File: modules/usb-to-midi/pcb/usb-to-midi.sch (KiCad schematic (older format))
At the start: 22 parts, among them J1 USB_B, J2 MIDI out, J3 DEBUG HEADER, U1 ATmega32U2-AU, Y1 16mhz

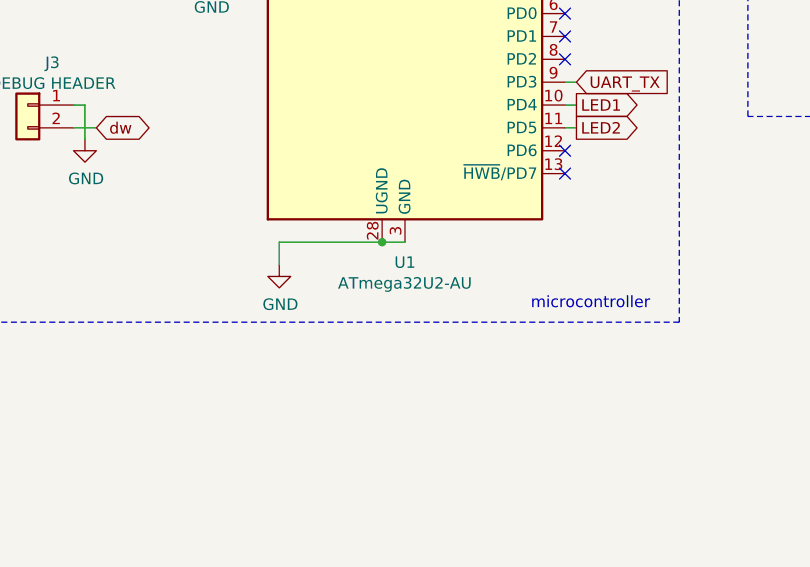
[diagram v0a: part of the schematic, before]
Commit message: usb-to-midi: fix some metadata, add schematic pdf
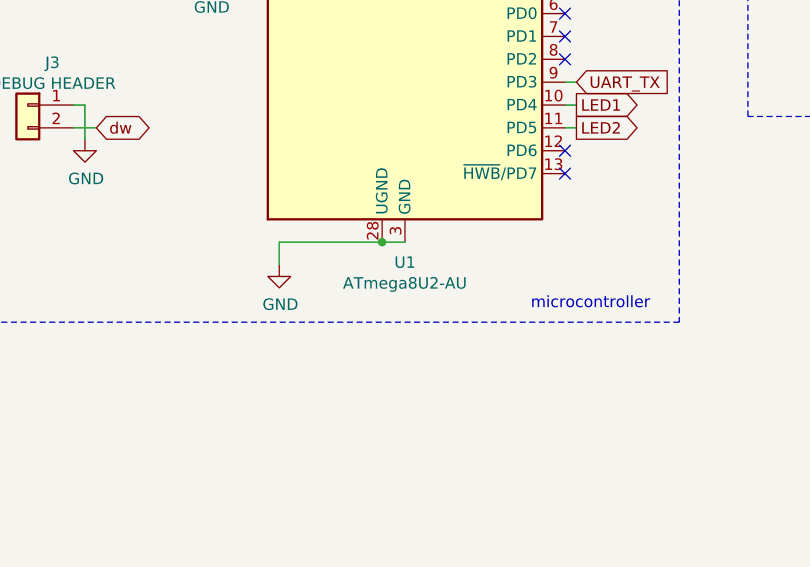
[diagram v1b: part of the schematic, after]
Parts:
- U1: value ATmega32U2-AU -> ATmega8U2-AU
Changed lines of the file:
@@
 encoding utf-8
 Sheet 1 1
-Title "usb-to-midi board"
+Title "usb-to-midi"
 Date "2021-12-13"
 Rev "1.0"
@@
 P 5800 3700
 F 0 "U1" H 5800 2211 50  0000 C CNN
-F 1 "ATmega32U2-AU" H 5800 2120 50  0000 C CNN
+F 1 "ATmega8U2-AU" H 5800 2120 50  0000 C CNN
 F 2 "eurorack:TQFP-32_7x7mm_P0.8mm_LongPads" H 5800 3700 50  0001 C CIN
 F 3 "http://ww1.microchip.com/downloads/en/DeviceDoc/doc7799.pdf" H 5800 3700 50  0001 C CNN

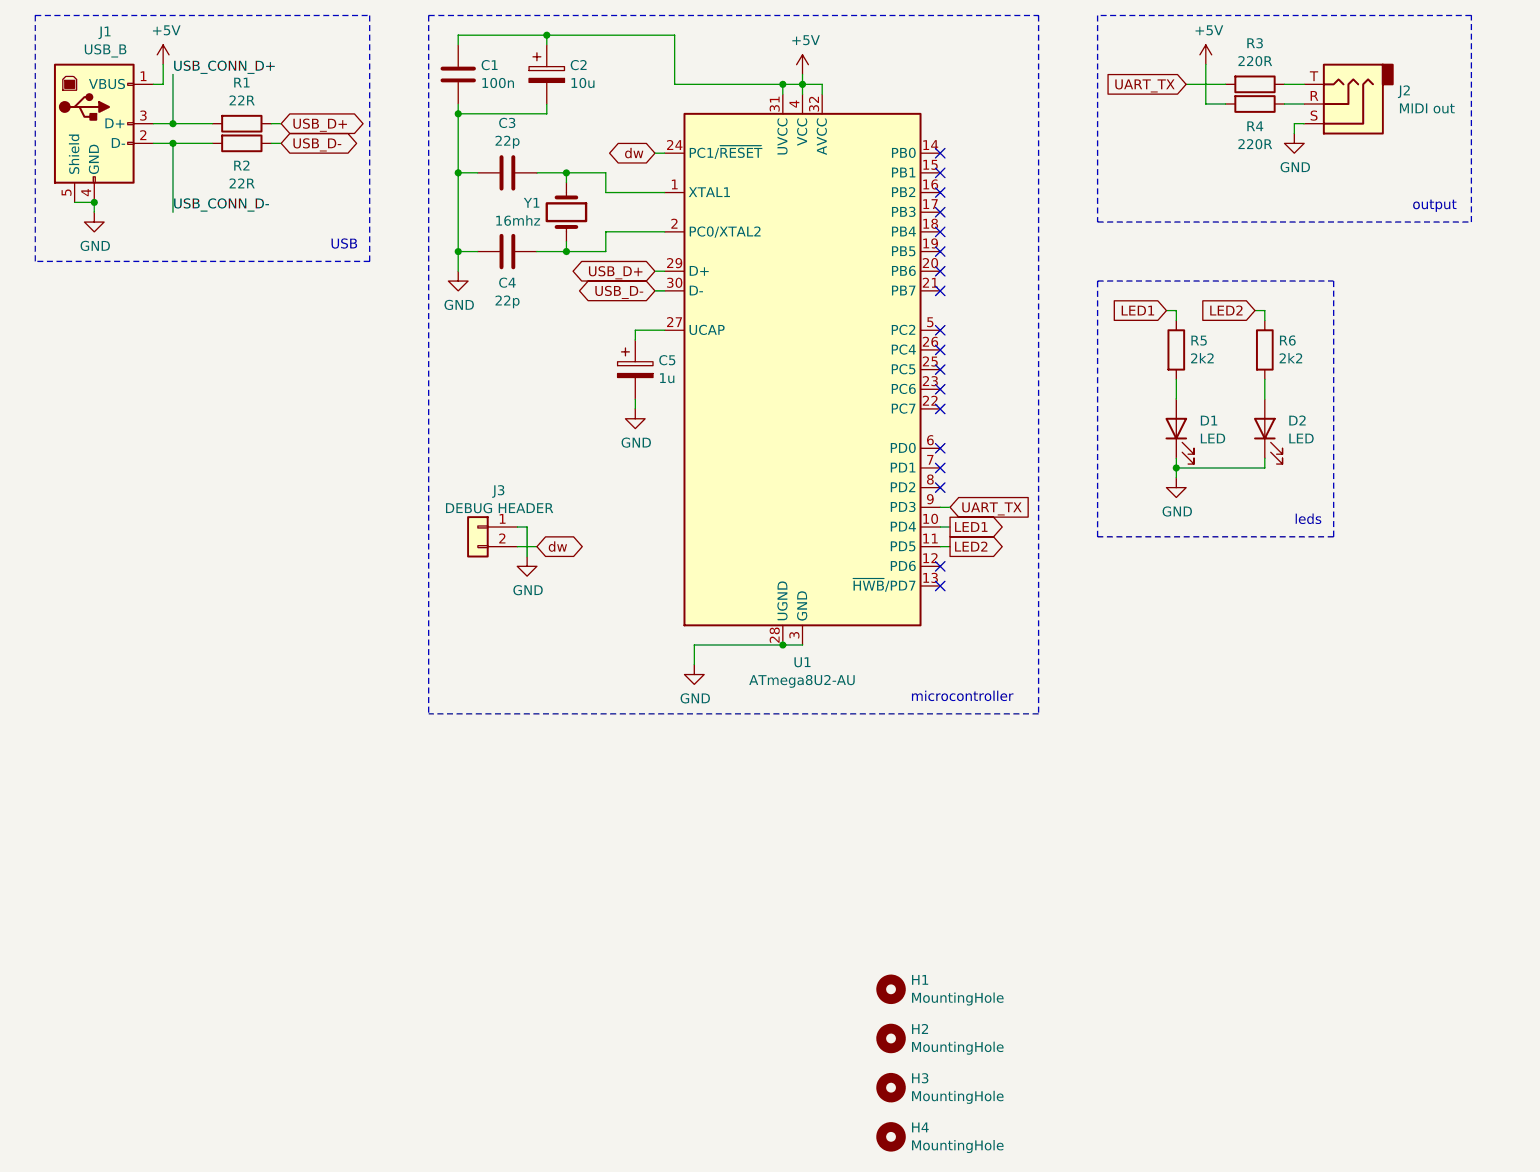
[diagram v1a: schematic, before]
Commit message: modules: usb-to-midi: fix references
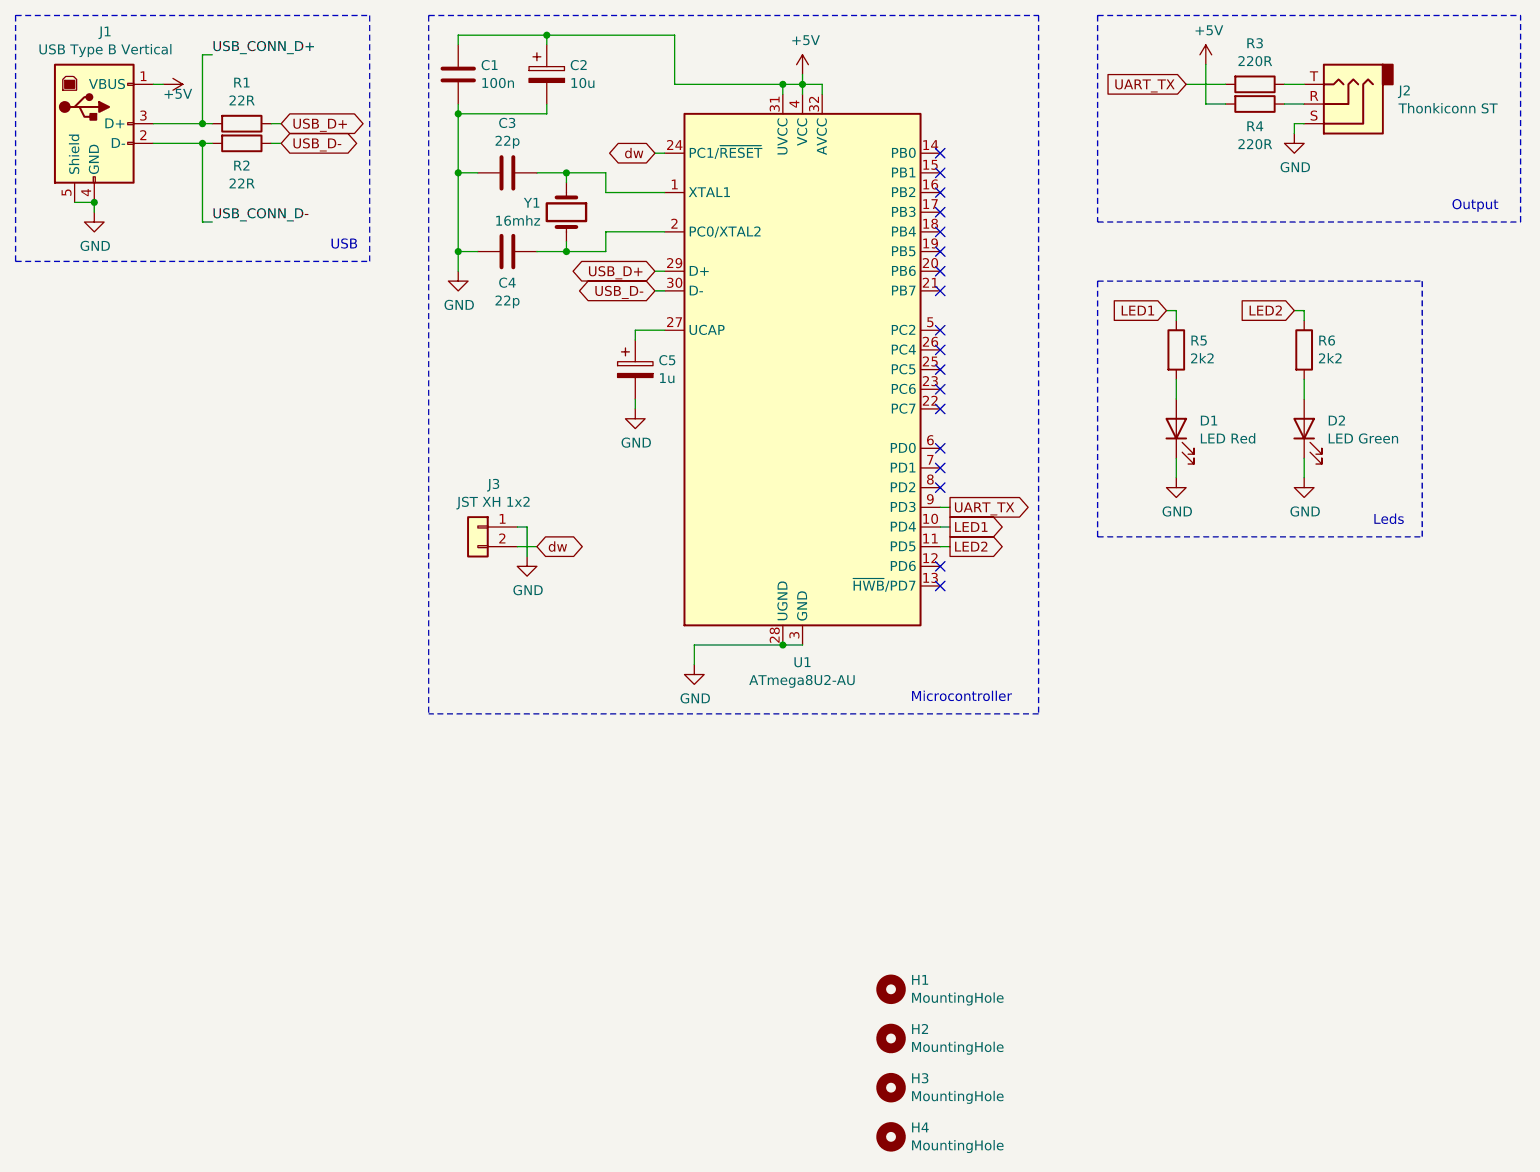
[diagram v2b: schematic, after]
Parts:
- D1: value LED -> LED Red
- D2: value LED -> LED Green
- J1: value USB_B -> USB Type B Vertical
- J2: value MIDI out -> Thonkiconn ST
- J3: value DEBUG HEADER -> JST XH 1x2
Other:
- note added: "Leds"
- note added: "Microcontroller"
- note added: "Output"
- note removed: "leds"
- note removed: "microcontroller"
- note removed: "output"
- moved on the sheet: D2, R6
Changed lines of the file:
@@
 	0    1    1    0
 $EndComp
-Text GLabel 6550 4400 2    50   Input ~ 0
+Text GLabel 6550 4400 2    50   Output ~ 0
 UART_TX
 $Comp
@@
 U 1 1 61353B09
 P 4150 4500
-F 0 "J3" H 4042 4685 50  0000 C CNN
-F 1 "DEBUG HEADER" H 4042 4594 50  0000 C CNN
+F 0 "J3" H 4068 4717 50  0000 C CNN
+F 1 "JST XH 1x2" H 4068 4626 50  0000 C CNN
 F 2 "Connector_JST:JST_XH_B2B-XH-A_1x02_P2.50mm_Vertical" H 4150 4500 50  0001 C CNN
 F 3 "~" H 4150 4500 50  0001 C CNN
@@
 P 7700 4000
 F 0 "D1" V 7739 3882 50  0000 R CNN
-F 1 "LED" V 7648 3882 50  0000 R CNN
+F 1 "LED Red" V 7648 3882 50  0000 R CNN
 F 2 "LED_THT:LED_D3.0mm" H 7700 4000 50  0001 C CNN
 F 3 "~" H 7700 4000 50  0001 C CNN
@@
 L Device:LED D2
 U 1 1 61C75707
-P 8150 4000
-F 0 "D2" V 8189 3882 50  0000 R CNN
-F 1 "LED" V 8098 3882 50  0000 R CNN
-F 2 "LED_THT:LED_D3.0mm" H 8150 4000 50  0001 C CNN
-F 3 "~" H 8150 4000 50  0001 C CNN
-	1    8150 4000
+P 8350 4000
+F 0 "D2" V 8389 3882 50  0000 R CNN
+F 1 "LED Green" V 8298 3882 50  0000 R CNN
+F 2 "LED_THT:LED_D3.0mm" H 8350 4000 50  0001 C CNN
+F 3 "~" H 8350 4000 50  0001 C CNN
+	1    8350 4000
 	0    -1   -1   0
 $EndComp
@@
 L Device:R R6
 U 1 1 61C770E0
-P 8150 3600
-F 0 "R6" H 8220 3646 50  0000 L CNN
-F 1 "2k2" H 8220 3555 50  0000 L CNN
-F 2 "Resistor_THT:R_Axial_DIN0207_L6.3mm_D2.5mm_P10.16mm_Horizontal" V 8080 3600 50  0001 C CNN
-F 3 "~" H 8150 3600 50  0001 C CNN
-	1    8150 3600
+P 8350 3600
+F 0 "R6" H 8420 3646 50  0000 L CNN
+F 1 "2k2" H 8420 3555 50  0000 L CNN
+F 2 "Resistor_THT:R_Axial_DIN0207_L6.3mm_D2.5mm_P10.16mm_Horizontal" V 8280 3600 50  0001 C CNN
+F 3 "~" H 8350 3600 50  0001 C CNN
+	1    8350 3600
 	1    0    0    -1
 $EndComp
 Text GLabel 7650 3400 0    50   Input ~ 0
 LED1
-Text GLabel 8100 3400 0    50   Input ~ 0
+Text GLabel 8300 3400 0    50   Input ~ 0
 LED2
 $Comp
@@
 	7700 3400 7700 3450
 Wire Wire Line
-	8100 3400 8150 3400
-Wire Wire Line
-	8150 3400 8150 3450
+	8300 3400 8350 3400
+Wire Wire Line
+	8350 3400 8350 3450
 Wire Wire Line
 	7700 3850 7700 3750
 Wire Wire Line
-	8150 3750 8150 3850
-Wire Wire Line
-	7700 4250 7700 4200
-Wire Wire Line
-	7700 4200 8150 4200
-Wire Wire Line
-	8150 4200 8150 4150
-Connection ~ 7700 4200
-Wire Wire Line
-	7700 4200 7700 4150
+	8350 3750 8350 3850
 NoConn ~ 6500 4200
 NoConn ~ 6500 4100
@@
 NoConn ~ 6500 3100
 NoConn ~ 6500 3600
-Text Notes 8900 2900 0    50   ~ 0
-output
-Wire Notes Line
-	8500 3250 8500 4550
-Text Notes 8300 4500 0    50   ~ 0
-leds
+Text Notes 9100 2900 0    50   ~ 0
+Output
+Wire Notes Line
+	8950 3250 8950 4550
+Text Notes 8700 4500 0    50   ~ 0
+Leds
 Wire Notes Line
 	7000 5450 3900 5450
@@
 Connection ~ 5700 5100
 Text Notes 6350 5400 0    50   ~ 0
-microcontroller
-Wire Notes Line
-	1900 1900 3600 1900
+Microcontroller
 Wire Notes Line
 	3600 1900 3600 3150
 Wire Notes Line
-	3600 3150 1900 3150
-Wire Notes Line
-	1900 3150 1900 1900
+	1800 3150 1800 1900
 Text Notes 3400 3100 0    50   ~ 0
 USB
-Text Label 2600 2200 0    50   ~ 0
+Text Label 2800 2100 0    50   ~ 0
 USB_CONN_D+
 Connection ~ 2200 2850
@@
 AR Path="/6175D50F/61C21FC1" Ref="J?"  Part="1"
 F 0 "J1" H 2257 2917 50  0000 C CNN
-F 1 "USB_B" H 2257 2826 50  0000 C CNN
+F 1 "USB Type B Vertical" H 2257 2826 50  0000 C CNN
 F 2 "eurorack:USB_B_Vertical" H 2350 2400 50  0001 C CNN
 F 3 " ~" H 2350 2400 50  0001 C CNN
@@
 	1    0    0    -1
 $EndComp
-Text Label 2600 2900 0    50   ~ 0
+Text Label 2800 2950 0    50   ~ 0
 USB_CONN_D-
-Wire Wire Line
-	2600 2900 2600 2550
-Wire Wire Line
-	2600 2550 2500 2550
-Wire Wire Line
-	2800 2550 2600 2550
-Connection ~ 2600 2550
-Wire Wire Line
-	2500 2450 2600 2450
-Wire Wire Line
-	2600 2200 2600 2450
-Connection ~ 2600 2450
-Wire Wire Line
-	2600 2450 2800 2450
 $Comp
 L power:GND #PWR0103
@@
 P 8550 2350
 F 0 "J2" H 8270 2283 50  0000 R CNN
-F 1 "MIDI out" H 8270 2374 50  0000 R CNN
+F 1 "Thonkiconn ST" H 8270 2374 50  0000 R CNN
 F 2 "eurorack:Jack_3.5mm_QingPu_WQP-PJ366ST_Vertical" H 8550 2350 50  0001 C CNN
 F 3 "~" H 8550 2350 50  0001 C CNN
@@
 NoConn ~ 6500 4800
 Wire Notes Line
-	9200 2950 9200 1900
-Wire Notes Line
-	9200 1900 7300 1900
+	9450 2950 9450 1900
 Wire Notes Line
 	7300 1900 7300 2950
 Wire Notes Line
-	7300 2950 9200 2950
-Wire Notes Line
-	8500 4550 7300 4550
-Wire Notes Line
 	7300 4550 7300 3250
-Wire Notes Line
-	7300 3250 8500 3250
-$Comp
-L power:+5V #PWR0107
-U 1 1 61655010
-P 2550 2150
-F 0 "#PWR0107" H 2550 2000 50  0001 C CNN
-F 1 "+5V" H 2565 2323 50  0000 C CNN
-F 2 "" H 2550 2150 50  0001 C CNN
-F 3 "" H 2550 2150 50  0001 C CNN
-	1    2550 2150
-	1    0    0    -1
-$EndComp
 Wire Wire Line
 	2500 2250 2550 2250
-Wire Wire Line
-	2550 2250 2550 2150
 Wire Wire Line
 	6500 4600 6550 4600
@@
 Wire Notes Line
 	3900 1900 3900 5450
+Wire Wire Line
+	2500 2550 2750 2550
+Wire Wire Line
+	2500 2450 2750 2450
+$Comp
+L power:+5V #PWR0107
+U 1 1 61655010
+P 2550 2250
+F 0 "#PWR0107" H 2550 2100 50  0001 C CNN
+F 1 "+5V" V 2600 2250 50  0000 L CNN
+F 2 "" H 2550 2250 50  0001 C CNN
+F 3 "" H 2550 2250 50  0001 C CNN
+	1    2550 2250
+	0    1    1    0
+$EndComp
+Wire Wire Line
+	2750 2450 2750 2100
+Wire Wire Line
+	2750 2100 2800 2100
+Connection ~ 2750 2450
+Wire Wire Line
+	2750 2450 2800 2450
+Wire Wire Line
+	2750 2550 2750 2950
+Wire Wire Line
+	2750 2950 2800 2950
+Connection ~ 2750 2550
+Wire Wire Line
+	2750 2550 2800 2550
+Wire Notes Line
+	1800 1900 3600 1900
+Wire Notes Line
+	1800 3150 3600 3150
+Wire Notes Line
+	7300 3250 8950 3250
+Wire Notes Line
+	7300 4550 8950 4550
+Wire Notes Line
+	7300 2950 9450 2950
+Wire Notes Line
+	7300 1900 9450 1900
+Wire Wire Line
+	7700 4150 7700 4250
+$Comp
+L power:GND #PWR?
+U 1 1 61D92920
+P 8350 4250
+F 0 "#PWR?" H 8350 4000 50  0001 C CNN
+F 1 "GND" H 8355 4077 50  0000 C CNN
+F 2 "" H 8350 4250 50  0001 C CNN
+F 3 "" H 8350 4250 50  0001 C CNN
+	1    8350 4250
+	1    0    0    -1
+$EndComp
+Wire Wire Line
+	8350 4150 8350 4250
 $EndSCHEMATC
